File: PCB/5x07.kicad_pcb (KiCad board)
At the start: 2 copper layers, 168.3 x 103.2 mm, 135 parts, among them J1 AVR-ISP-6, J2 AudioJack3_Ground, K0 KC_ESC, K1 KC_GRV, K10 SW_Push, K11 KC_TAB, K12 KC_Q, K13 KC_W, K14 KC_E, K15 KC_R, K16 KC_T, K2 KC_1, K20 SW_Push, K21 KC_CAPS, K22 KC_A, K23 KC_S, K24 KC_D, K25 KC_F, K26 KC_G, K3 KC_2, K30 SW_Push, K31 KC_LSFT, K32 KC_Z, K33 KC_X, K34 KC_C, K35 KC_V, K36 KC_B, K4 KC_3, K40 SW_Push, K41 KC_LCTL, K42 KC_LGUI, K43 KC_LALT, K44 KC_FN, K45 KC_SPACE, K46 KC_SPACE, K5 KC_4, K6 KC_5, SW1 SW_Push, U1 ATmega32U4-A, U2 PRTR5V0U2X, Y1 16MHz

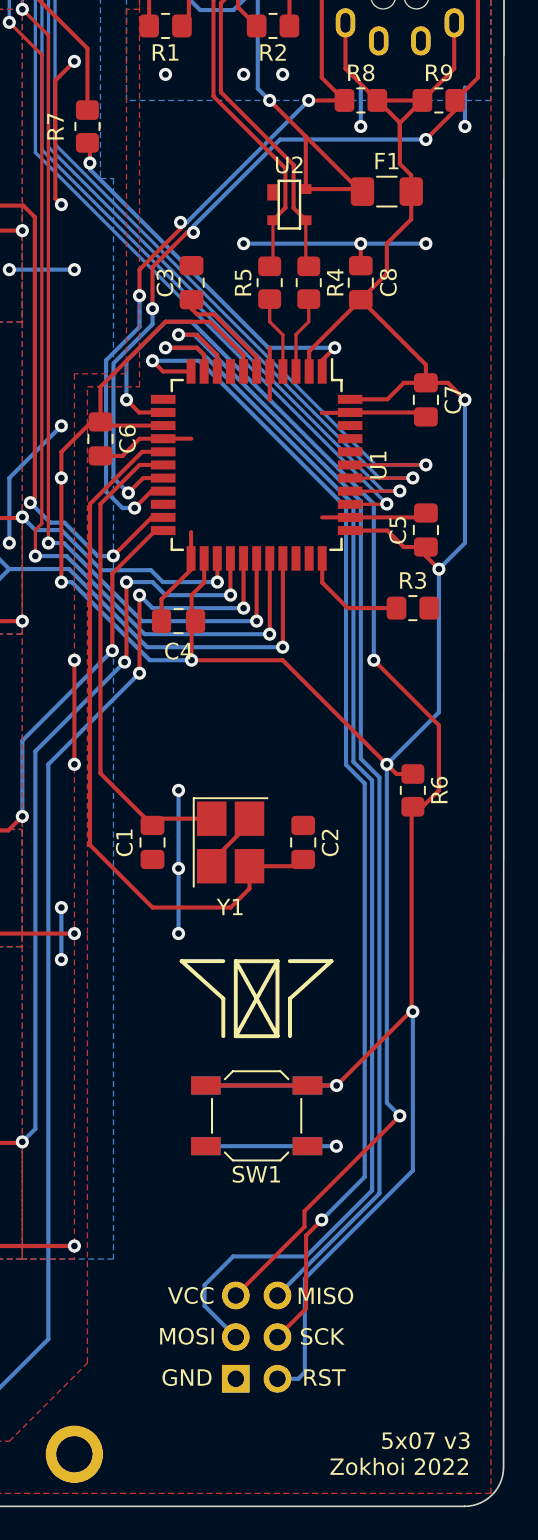
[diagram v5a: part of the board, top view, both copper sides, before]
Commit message: added vbus detection compatibility
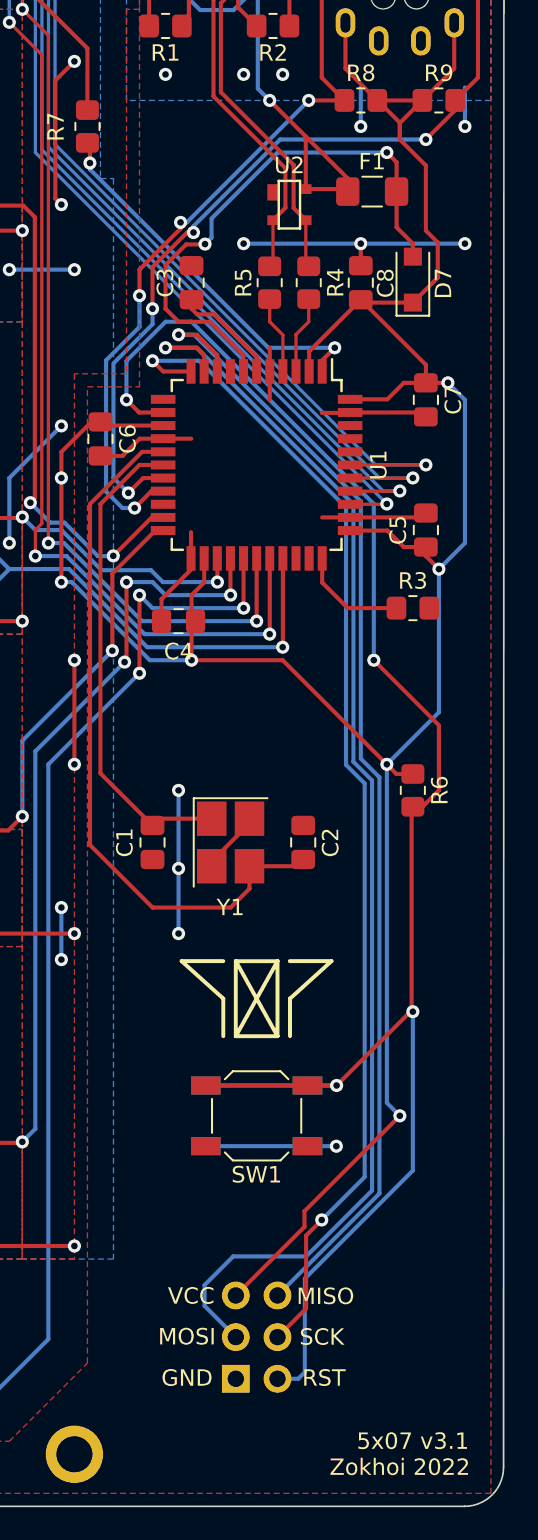
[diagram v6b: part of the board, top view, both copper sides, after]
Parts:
- added D7: D_Schottky, Diode_SMD:D_SOD-123F, F.Cu at (215.1, 58.5)
- moved F1 0.89 mm to (212.6, 53.2)
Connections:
- F1 pad 2: +5V -> VBUS
- U1 pad 7: +5V -> VBUS
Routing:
- net VBUS: track 0.00 -> 33.6 mm, vias 0 -> 2
- net +5V: track 340.2 -> 329.3 mm
- net GND: track 193.5 -> 195.8 mm
- net VCC: track 36.8 -> 35.3 mm
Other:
- board text added: "5x07 v3.1"
- board text removed: "5x07 v3"
